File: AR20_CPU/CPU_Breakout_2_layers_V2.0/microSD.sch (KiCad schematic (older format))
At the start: 1 part

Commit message: Push button edited
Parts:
- added C12: 10u, Capacitor_SMD:C_0603_1608Metric_Pad1.05x0.95mm_HandSolder, symbol Device:C
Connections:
- net 3.3V: now also C12.1
- net Ground: now also C12.2
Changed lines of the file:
@@
 Wire Wire Line
 	5350 3500 5350 3750
+$Comp
+L Device:C C12
+U 1 1 5E66571C
+P 5100 4500
+F 0 "C12" H 5215 4546 50  0000 L CNN
+F 1 "10u" H 5215 4455 50  0000 L CNN
+F 2 "Capacitor_SMD:C_0603_1608Metric_Pad1.05x0.95mm_HandSolder" H 5138 4350 50  0001 C CNN
+F 3 "~" H 5100 4500 50  0001 C CNN
+	1    5100 4500
+	1    0    0    -1
+$EndComp
+Text GLabel 5100 4200 0    50   Input ~ 0
+3.3V
+Text GLabel 5100 4800 0    50   Input ~ 0
+Ground
+Wire Wire Line
+	5100 4800 5100 4650
+Wire Wire Line
+	5100 4200 5100 4350
 $EndSCHEMATC

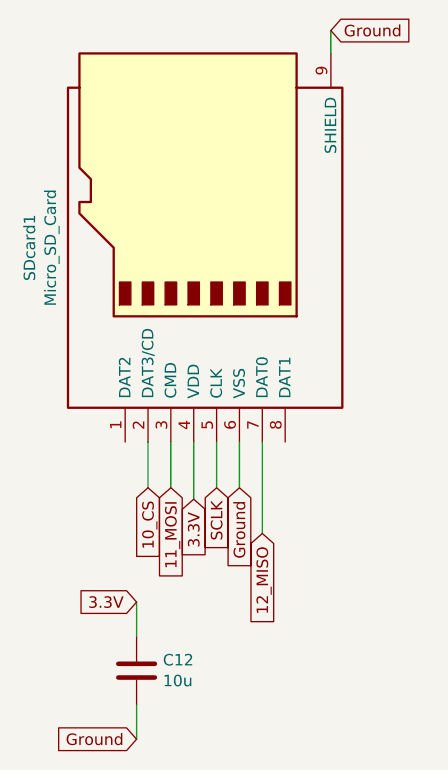
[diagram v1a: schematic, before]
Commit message: Endret SCLK pin til SD
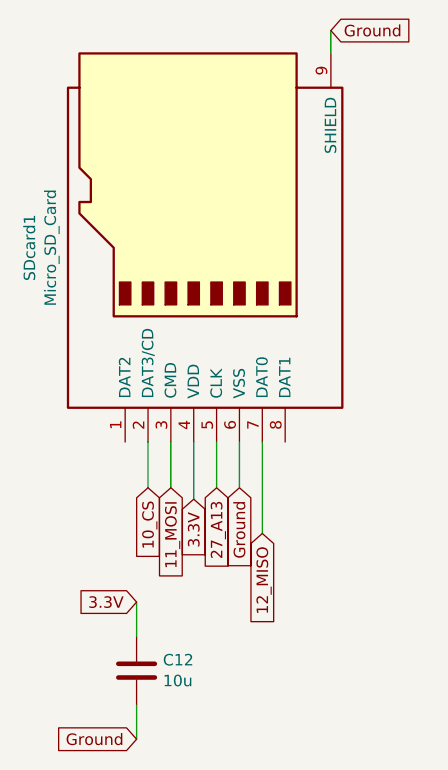
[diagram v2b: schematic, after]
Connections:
- net SCLK renamed 27_A13
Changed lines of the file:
@@
 Text GLabel 5150 3700 3    50   Input ~ 0
 10_CS
-Text GLabel 5450 3700 3    50   Input ~ 0
-SCLK
 Text GLabel 5250 3700 3    50   Input ~ 0
 11_MOSI
@@
 Wire Wire Line
 	5100 4200 5100 4350
+Text GLabel 5450 3700 3    50   Input ~ 0
+27_A13
 $EndSCHEMATC
